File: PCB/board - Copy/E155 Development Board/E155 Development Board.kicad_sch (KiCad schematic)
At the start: 46 parts, among them J1 Screw_Terminal_01x02, J2 Conn_01x03, J3 Conn_01x02, J4 Conn_01x02, J6 Conn_02x20_Odd_Even, J7 Conn_01x06, SW0 SW_Push, SW1 SW_Push, SW2 SW_Push, SW3 SW_Push, SW4 SW_Push, SW5 SW_Push, SW6 SW_DIP_x04, SW7 SW_DIP_x08, U1 NUCLEO-LxxxKx, U2 UPduino_v3.1, U3 LD1117DT50TR, U4 LD1117DT33CTR, U5 mikroBUS_SOCKET

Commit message: Schematic Changes
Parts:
- removed D4, D5: LED (G), LED_SMD:LED_0805_2012Metric_Pad1.15x1.40mm_HandSolder, symbol Device:LED
- removed D6, D7, D8: LED (B), LED_SMD:LED_0805_2012Metric_Pad1.15x1.40mm_HandSolder, symbol Device:LED
- removed J2: Conn_01x03, Connector_PinHeader_2.54mm:PinHeader_1x03_P2.54mm_Vertical, symbol Connector_Generic:Conn_01x03
- removed J6: Conn_02x20_Odd_Even, E155_Footprints:2x20 Pin Header Keyed, symbol Connector_Generic:Conn_02x20_Top_Bottom
- removed J7: Conn_01x06, Connector_PinSocket_2.54mm:PinSocket_1x06_P2.54mm_Vertical, symbol Connector_Generic:Conn_01x06
- removed R10, R11, R7, R8, R9: 1k, Resistor_SMD:R_0805_2012Metric_Pad1.20x1.40mm_HandSolder, symbol Device:R_US
- removed SW0, SW1, SW2, SW3: SW_Push, Button_Switch_THT:SW_PUSH_6mm_H4.3mm, symbol Switch:SW_Push
- removed SW6: SW_DIP_x04, Button_Switch_THT:SW_DIP_SPSTx04_Slide_6.7x11.72mm_W7.62mm_P2.54mm_LowProfile, symbol Switch:SW_DIP_x04
- added J2: Conn_01x02, symbol Connector_Generic:Conn_01x02
- D3: value LED (G) -> LED (B)
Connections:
- net +3V3: now also D3.2 (A)
- net +5V: now also D2.2 (A)
- net MIKROBUS_RST: now also J2.2 (Pin_2)
- net P10: no longer SW7.11
- net P12: no longer SW7.10
- net P20: no longer SW7.12
- net P21: no longer SW7.9
- net P23: no longer SW7.16
- net P25: no longer SW7.15
- net P26: no longer SW7.14
- net P27: no longer SW7.13
- net PA10: no longer D2.2 (A), SW7.1
- net PA11: no longer SW7.5
- net PA5: no longer SW7.3
- net PA6: no longer SW7.4
- net PA9: no longer D3.2 (A), SW7.2
- net PB3: no longer SW7.8
- net PB4: no longer SW7.7
- net PB5: no longer SW7.6
- net at R3.2: now also J2.1 (Pin_1)
- net VIN renamed BATT
- new net TBD: SW7.1, SW7.10, SW7.11, SW7.12, SW7.13, SW7.14, SW7.15, SW7.16, SW7.2, SW7.3, SW7.4, SW7.5, SW7.6, SW7.7, SW7.8, SW7.9
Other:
- note added: "3V3"
- note added: "5V"
- note removed: "DIP Switches (Use Internal Pull-up Resistors)"
- note removed: "PMOD Connector"
- note removed: "Push Buttons (Use Internal Pull-up Resistors)"
- note removed: "RX"
- note removed: "SCK"
- note removed: "SCL"
- note removed: "TX"

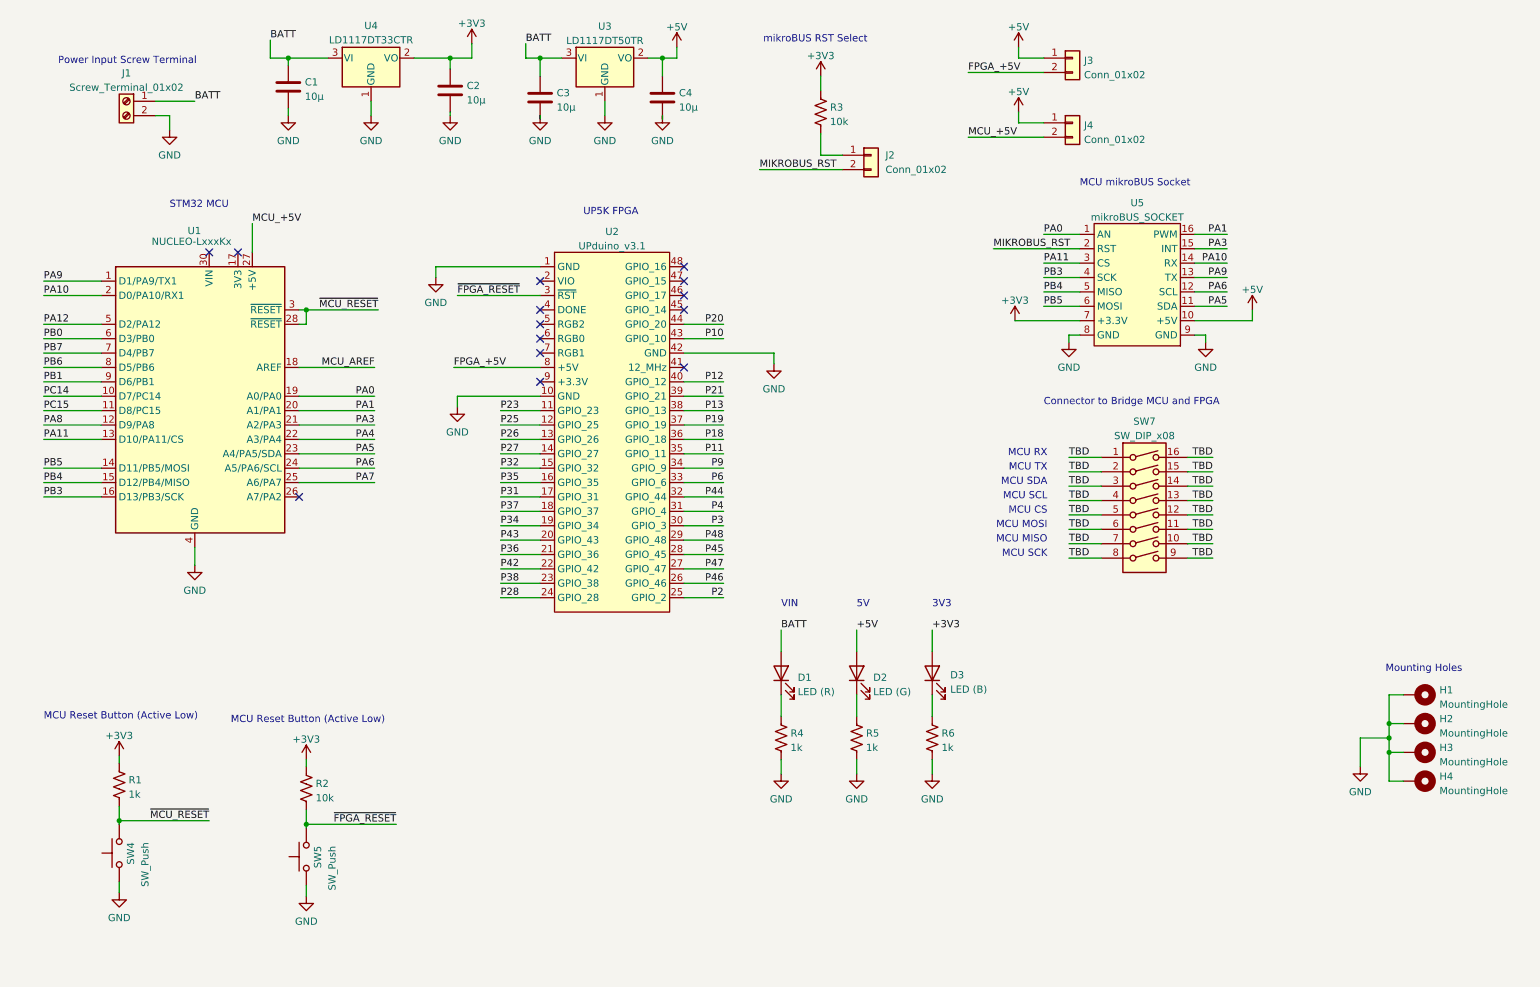
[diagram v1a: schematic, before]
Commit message: Reformatted schematic, added speaker amp hierarchal sheet
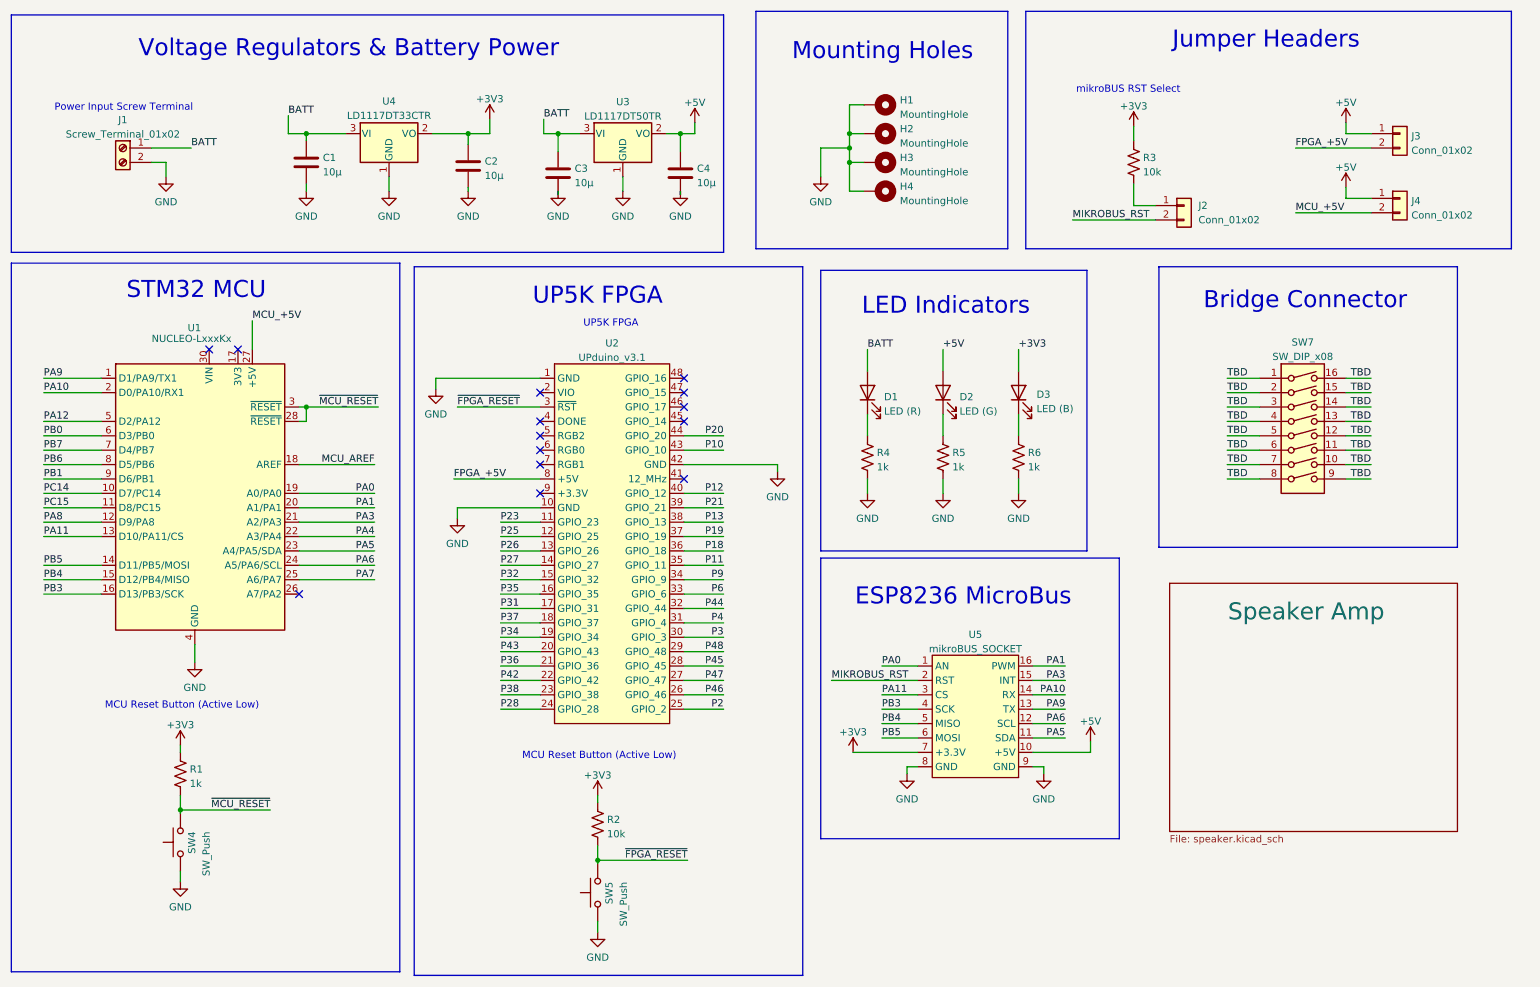
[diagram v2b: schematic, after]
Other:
- added sheet Speaker Amp (speaker.kicad_sch)
- note added: "Bridge Connector"
- note added: "ESP8236 MicroBus"
- note added: "Jumper Headers"
- note added: "LED Indicators"
- note added: "Voltage Regulators & Battery Power"
- note removed: "3V3"
- note removed: "5V"
- note removed: "Connector to Bridge MCU and FPGA"
- note removed: "MCU CS"
- note removed: "MCU MISO"
- note removed: "MCU MOSI"
- note removed: "MCU RX"
- note removed: "MCU SCK"
- note removed: "MCU SCL"
- note removed: "MCU SDA"
- note removed: "MCU TX"
- note removed: "MCU mikroBUS Socket"
- note removed: "VIN"
- moved on the sheet: C1, C2, C3, C4, D1, D2, D3, H1, H2, H3, H4, J1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

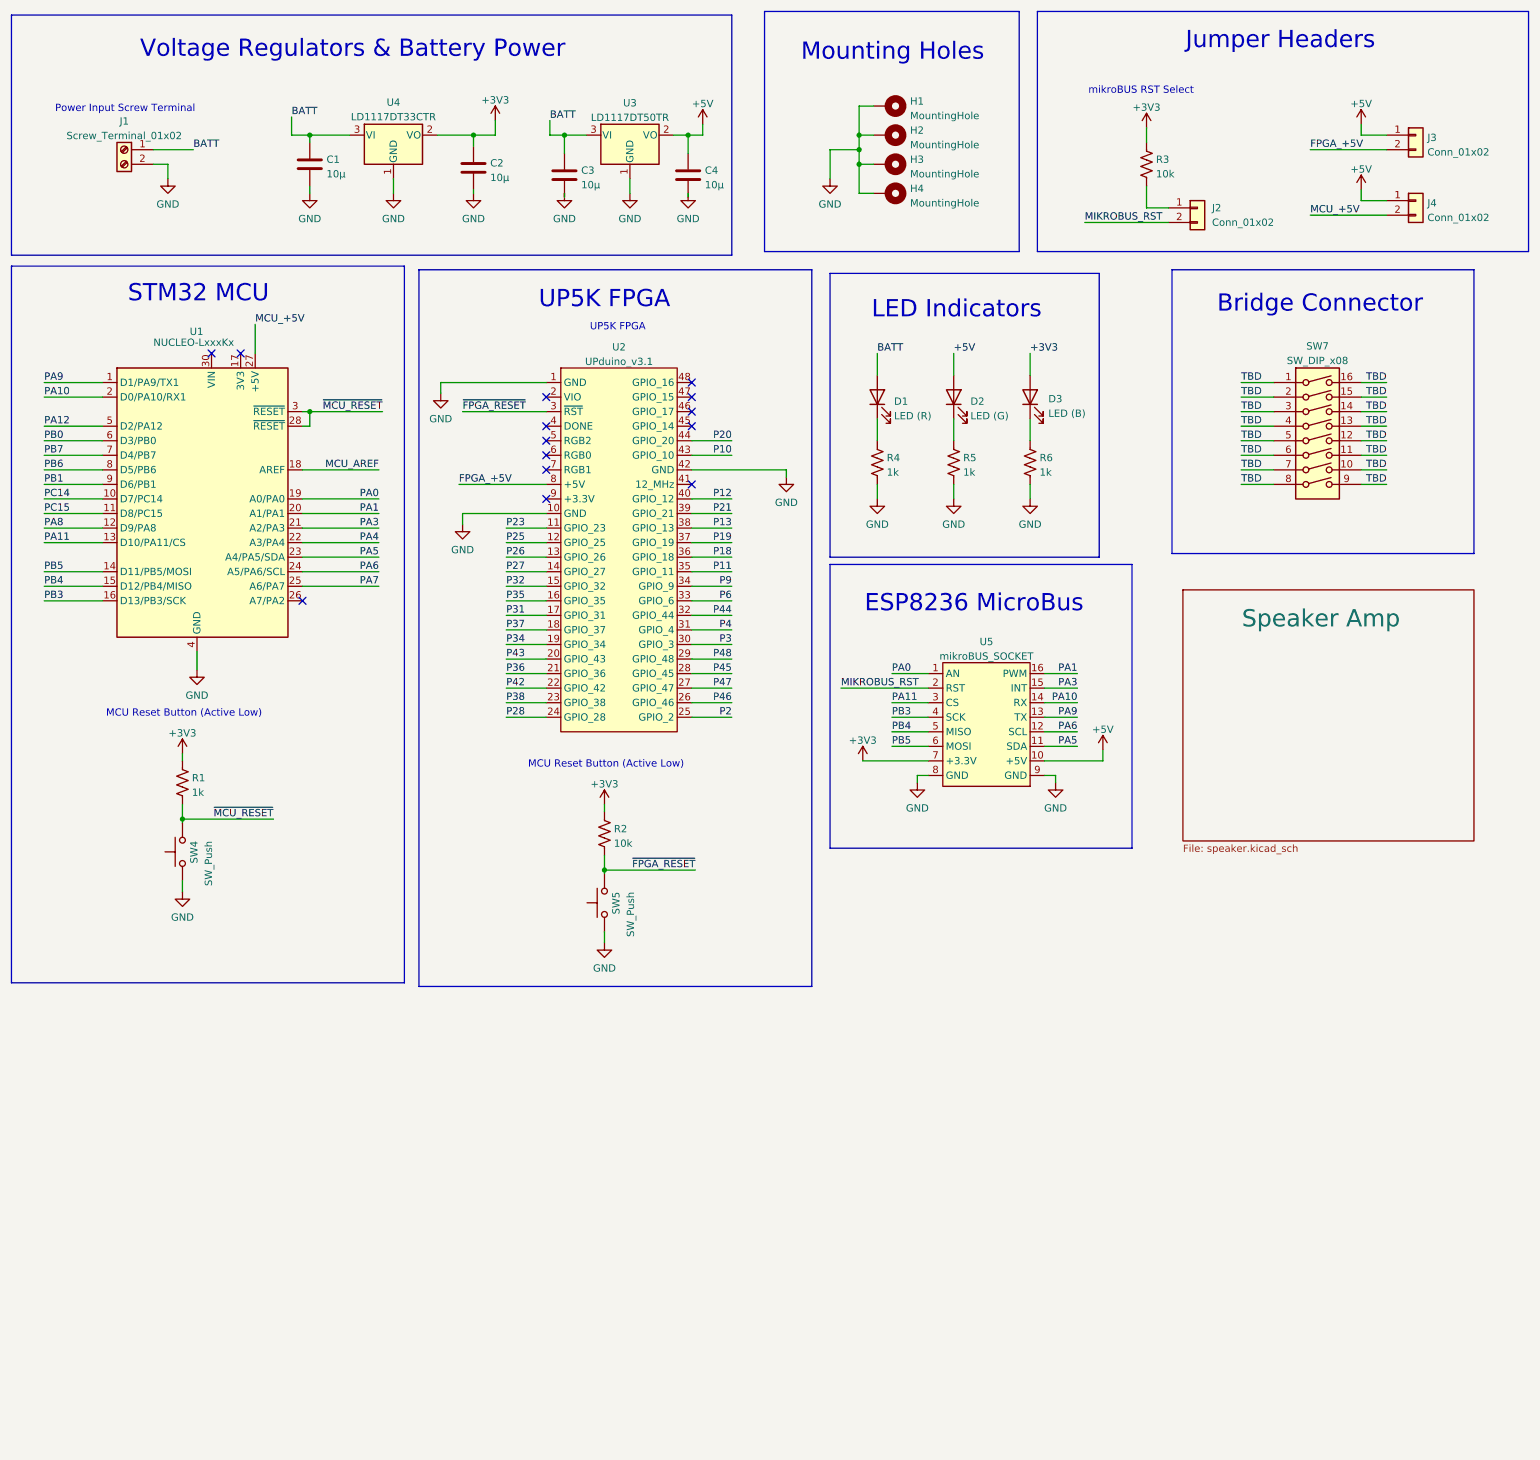
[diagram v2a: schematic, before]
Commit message: Increased Schematic Size, Added audio amplifier and temporary IR LED circuits
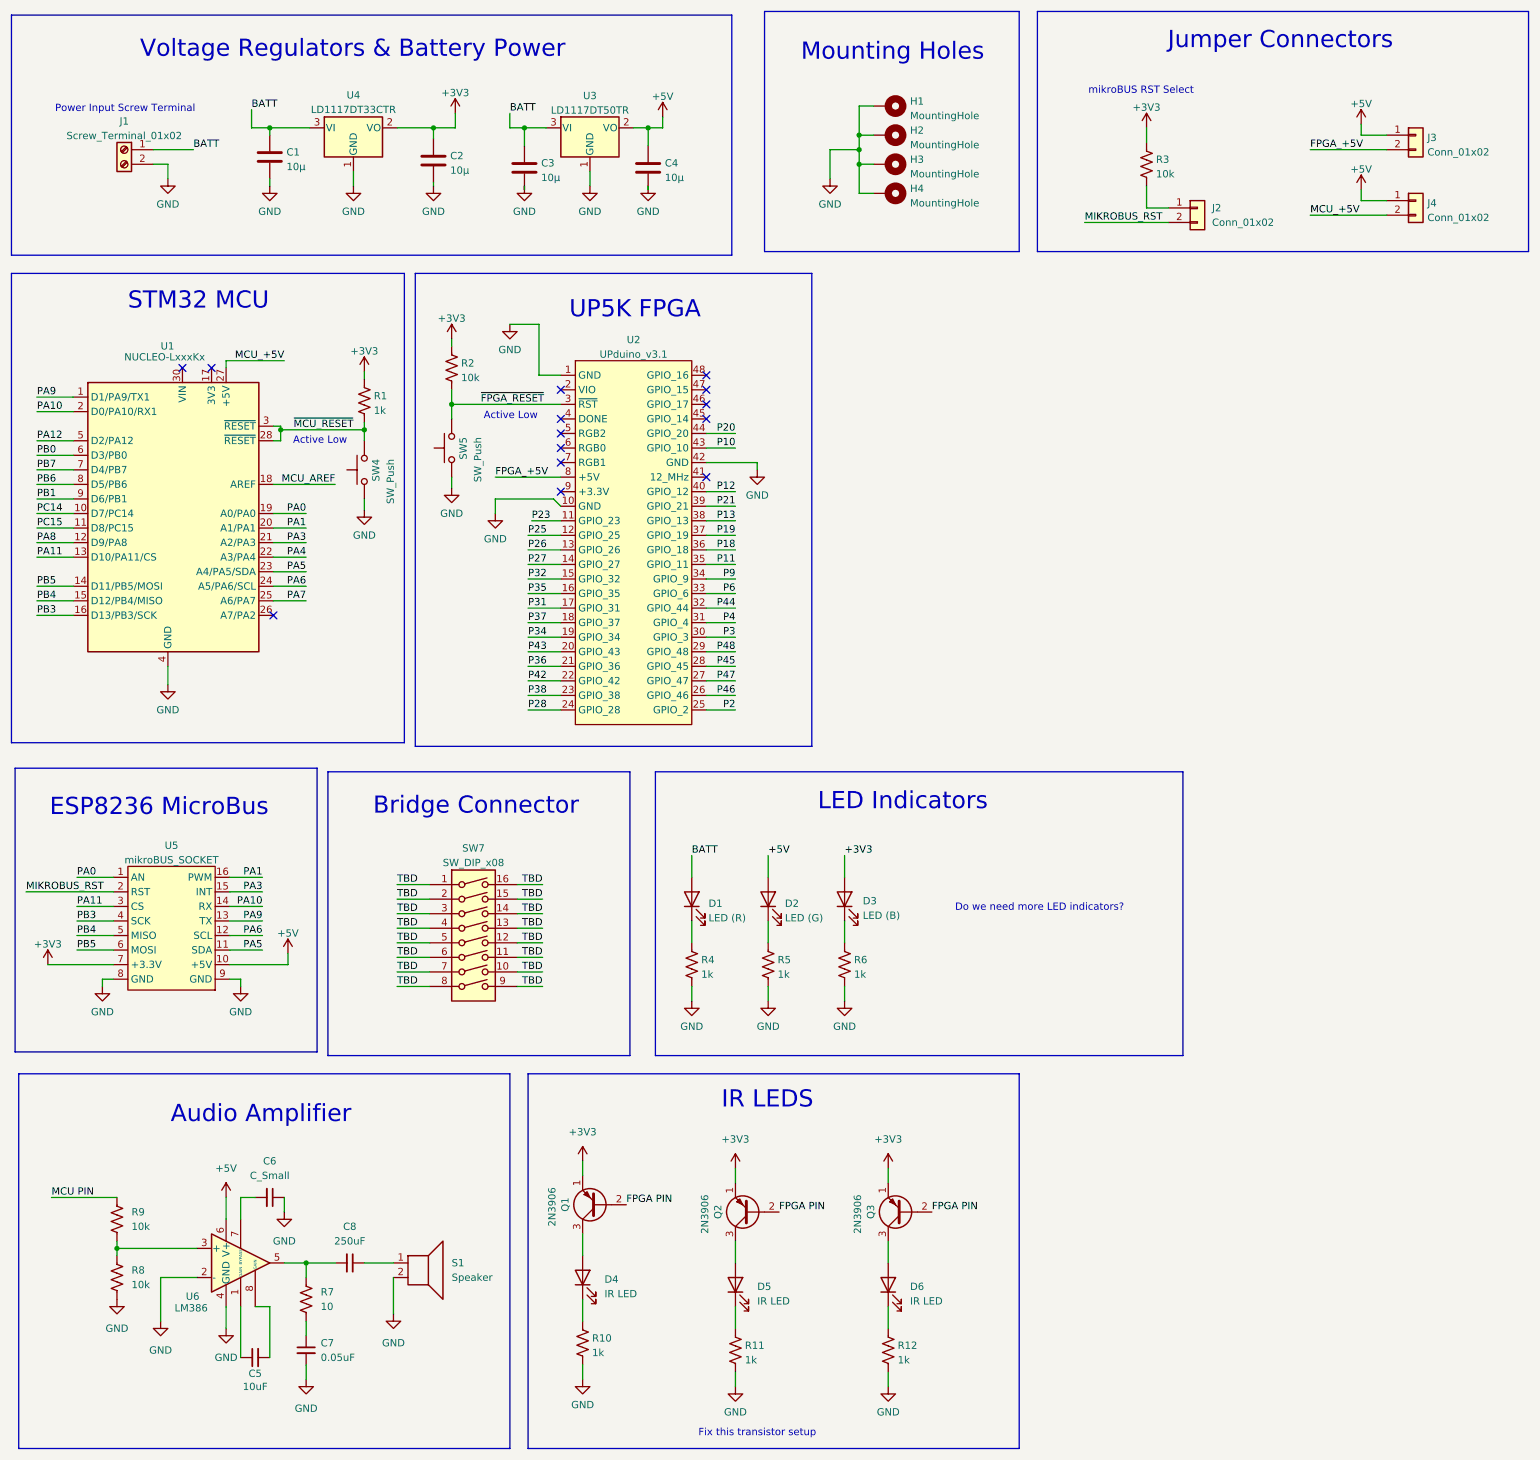
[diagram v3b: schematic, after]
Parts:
- added C5: 10uF, symbol Device:C_Small
- added C6: C_Small, symbol Device:C_Small
- added C7: 0.05uF, symbol Device:C_Small
- added C8: 250uF, symbol Device:C_Small
- added D4, D5, D6: IR LED, LED_SMD:LED_0805_2012Metric_Pad1.15x1.40mm_HandSolder, symbol Device:LED
- added Q1, Q2, Q3: 2N3906, Package_TO_SOT_THT:TO-92_Inline, symbol Transistor_BJT:2N3906
- added R10, R11, R12: 1k, Resistor_SMD:R_0805_2012Metric_Pad1.20x1.40mm_HandSolder, symbol Device:R_US
- added R7: 10, Resistor_SMD:R_0805_2012Metric_Pad1.20x1.40mm_HandSolder, symbol Device:R_US
- added R8, R9: 10k, Resistor_SMD:R_0805_2012Metric_Pad1.20x1.40mm_HandSolder, symbol Device:R_US
- added S1: Speaker, symbol Device:Speaker
- added U6: LM386, symbol Amplifier_Audio:LM386
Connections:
- net +3V3: now also Q1.1 (E), Q2.1 (E), Q3.1 (E)
- net +5V: now also U6.6 (V+)
- net GND: now also C6.1, C7.2, R10.2, R11.2, R12.2, R8.2, S1.2, U6.2 (-), U6.4 (GND)
- new net: R8.1, R9.2, U6.3 (+)
- new net: D5.1 (K), R11.1
- new net: C6.2, U6.7 (BYPASS)
- new net: D5.2 (A), Q2.3 (C)
- new net: C8.1, S1.1
- new net: C8.2, R7.1, U6.5
- new net: D4.1 (K), R10.1
- new net: D6.1 (K), R12.1
- new net: C5.1, U6.1 (GAIN)
- new net: C5.2, U6.8 (GAIN)
- new net: D4.2 (A), Q1.3 (C)
- new net: D6.2 (A), Q3.3 (C)
- new net: C7.1, R7.2
- new net FPGA PIN: Q1.2 (B), Q2.2 (B), Q3.2 (B)
- new net MCU PIN: R9.1
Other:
- removed sheet Speaker Amp
- note added: "Active Low"
- note added: "Audio Amplifier"
- note added: "Do we need more LED indicators?"
- note added: "Fix this transistor setup"
- note added: "IR LEDS"
- note added: "Jumper Connectors"
- note removed: "Jumper Headers"
- note removed: "MCU Reset Button (Active Low)"
- moved on the sheet: C1, C2, C3, C4, D1, D2, D3, R1, R2, R4, R5, R6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

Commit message: Initialized CAD file
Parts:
- removed D5, D6: IR LED, LED_SMD:LED_0805_2012Metric_Pad1.15x1.40mm_HandSolder, symbol Device:LED
- removed Q2, Q3: 2N3906, Package_TO_SOT_THT:TO-92_Inline, symbol Transistor_BJT:2N3906
- removed R12: 1k, Resistor_SMD:R_0805_2012Metric_Pad1.20x1.40mm_HandSolder, symbol Device:R_US
- added J5: 3V7 Lipo 1, Connector_JST:JST_PH_B2B-PH-K_1x02_P2.00mm_Vertical, symbol Connector_Generic:Conn_01x02
- added J6: 3V7 Lipo 2, Connector_JST:JST_PH_B2B-PH-K_1x02_P2.00mm_Vertical, symbol Connector_Generic:Conn_01x02
- added SW6: SW_Push, Button_Switch_THT:SW_PUSH_6mm_H4.3mm, symbol Switch:SW_Push
- added U7, U8, U9: TSSP6P38, OptoDevice:Vishay_MINICAST-3Pin, symbol Sensor_Proximity:TSSP58038
- J2: value Conn_01x02 -> ESP RST Jumper
- J3: value Conn_01x02 -> FPGA Jumper
- J4: value Conn_01x02 -> MCU Jumper
- R11: value 1k -> 10k
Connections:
- net +3V3: now also U7.3 (Vs), U8.3 (Vs), U9.3 (Vs)
- net +5V: now also R11.1
- net FPGA PIN: now also U7.1 (OUT), U8.1 (OUT), U9.1 (OUT)
- net GND: now also J6.2 (Pin_2), SW6.1, U7.2 (GND), U8.2 (GND), U9.2 (GND); no longer R11.2
- new net BATT_MID: J5.2 (Pin_2), J6.1 (Pin_1)
- new net BATT_RAW: J5.1 (Pin_1)
- new net FPGA Pin: R11.2, SW6.2
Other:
- note added: "Battery Management"
- note added: "ESP8266 MicroBus"
- note added: "IR Setup"
- note removed: "ESP8236 MicroBus"
- note removed: "IR LEDS"
- note removed: "mikroBUS RST Select"
- moved on the sheet: J2, R3
